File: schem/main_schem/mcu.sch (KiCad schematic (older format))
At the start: 40 parts, among them P2 CONN_PORTD, P3 CONN_ICD, P4 CONN_NFC, P5 CONN_2, Q2 NPN, SW1 SW_RESET, U4 25LC256, U5 PIC18F97J60, X1 25MHz

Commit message: Switch NFC comm from SPI to I2C
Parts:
- added R? (x2): 3.3k, symbol R
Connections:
- net +3.3V: now also R?.1, R?.1
- net SCK1: no longer P4.2 (P2)
- net SDO1: no longer P4.4 (P4)
- net SCL: now reaches P2.6 (P6), U5.84 (RD6/AD6/PSP6/SCK2/SCL2)
- net SCL: now also P4.2 (P2), R?.2
- net SCA: now reaches P2.7 (P7), U5.87 (RD5/AD5/PSP5/SDI2/SDA2)
- net SCA: now also P4.4 (P4), R?.2
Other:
- note removed: "FLIPS RX POLARITY OF ETHERNET"
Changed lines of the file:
@@
-EESchema Schematic File Version 2  date 10/8/2012 1:33:22 PM
+EESchema Schematic File Version 2  date 10/12/2012 9:52:20 AM
 LIBS:power
 LIBS:device
@@
 Sheet 4 6
 Title "MCU block"
-Date "8 oct 2012"
+Date "12 oct 2012"
 Rev "1"
 Comp "ECE 402 Senior Design, Ingersoll Rand Group"
@@
 Comment4 ""
 $EndDescr
-Text Notes 2000 2650 0    30   ~ 0
-for XC1671CT-ND:\n c_l = 18pF\n\nC7=C8=Cb\n\nCb / 2 + (2 to 5 pF) = cl\n27/2 + 3.5 = 17pF --> about 18 pF
-Text Notes 8900 3700 0    60   ~ 0
-BREAKOUT TO EXTERNAL NFC BOARD
+Connection ~ 8500 3700
+Wire Wire Line
+	8500 3700 8500 3650
+Connection ~ 7950 4300
+Wire Wire Line
+	7950 4300 8450 4300
+Wire Wire Line
+	8450 4300 8450 4250
+Wire Wire Line
+	8050 4500 8050 3250
+Connection ~ 7950 3350
 Wire Notes Line
 	11200 5150 8850 5150
@@
 Wire Notes Line
 	8850 3600 11200 3600
+Connection ~ 8050 3250
+Wire Wire Line
+	7950 4500 7950 3350
+Wire Wire Line
+	8600 4250 8600 4350
+Wire Wire Line
+	8600 4350 8050 4350
+Connection ~ 8050 4350
+Wire Wire Line
+	8450 3750 8450 3700
+Wire Wire Line
+	8450 3700 8600 3700
+Wire Wire Line
+	8600 3700 8600 3750
+$Comp
+L +3.3V #PWR?
+U 1 1 50782C27
+P 8500 3650
+F 0 "#PWR?" H 8500 3610 30  0001 C CNN
+F 1 "+3.3V" H 8500 3760 30  0000 C CNN
+	1    8500 3650
+	1    0    0    -1
+$EndComp
+$Comp
+L R R?
+U 1 1 50782BA9
+P 8450 4000
+F 0 "R?" V 8530 4000 50  0000 C CNN
+F 1 "3.3k" V 8450 4000 50  0000 C CNN
+	1    8450 4000
+	1    0    0    -1
+$EndComp
+$Comp
+L R R?
+U 1 1 50782B9F
+P 8600 4000
+F 0 "R?" V 8680 4000 50  0000 C CNN
+F 1 "3.3k" V 8600 4000 50  0000 C CNN
+	1    8600 4000
+	1    0    0    -1
+$EndComp
+Text GLabel 7950 4500 3    30   BiDi ~ 0
+SCA
+Text GLabel 8050 4500 3    30   Output ~ 0
+SCL
+$Comp
+L CONN_8 P2
+U 1 1 506EDDF7
+P 8500 3100
+F 0 "P2" V 8450 3100 60  0000 C CNN
+F 1 "CONN_PORTD" V 8550 3100 60  0000 C CNN
+	1    8500 3100
+	1    0    0    -1
+$EndComp
+Text Notes 2000 2650 0    30   ~ 0
+for XC1671CT-ND:\n c_l = 18pF\n\nC7=C8=Cb\n\nCb / 2 + (2 to 5 pF) = cl\n27/2 + 3.5 = 17pF --> about 18 pF
+Text Notes 8900 3700 0    60   ~ 0
+BREAKOUT TO EXTERNAL NFC BOARD
 Text Notes 5150 7050 0    60   ~ 0
 4kHz PWM sig
@@
 NFC_SELECT_NOT
 Text GLabel 10050 4400 0    60   BiDi ~ 0
-SDO1
+SCA
 Text GLabel 10050 4250 0    60   BiDi ~ 0
 SDI1
 Text GLabel 10050 4100 0    60   BiDi ~ 0
-SCK1
-$Comp
-L CONN_8 P2
-U 1 1 506EDDF7
-P 8500 3100
-F 0 "P2" V 8450 3100 60  0000 C CNN
-F 1 "CONN_PORTD" V 8550 3100 60  0000 C CNN
-	1    8500 3100
-	1    0    0    -1
-$EndComp
+SCL
 $Comp
 L VSS #PWR48
@@
 NoConn ~ 7100 4500
 NoConn ~ 7100 4450
-Text Notes 7300 3950 0    30   ~ 0
-FLIPS RX POLARITY OF ETHERNET
 Text GLabel 7500 4000 2    30   Output ~ 0
 RXSWAP

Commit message: Switch NFC comm from SPI to I2C
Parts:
- gave numbers to parts that had none: 2
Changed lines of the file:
@@
-EESchema Schematic File Version 2  date 10/12/2012 9:52:20 AM
+EESchema Schematic File Version 2  date 10/12/2012 10:11:24 AM
 LIBS:power
 LIBS:device
@@
 Comment4 ""
 $EndDescr
+Text GLabel 10050 4250 0    60   BiDi ~ 0
+SDI1
 Connection ~ 8500 3700
 Wire Wire Line
@@
 	8600 3700 8600 3750
 $Comp
-L +3.3V #PWR?
+L +3.3V #PWR49
 U 1 1 50782C27
 P 8500 3650
-F 0 "#PWR?" H 8500 3610 30  0001 C CNN
+F 0 "#PWR49" H 8500 3610 30  0001 C CNN
 F 1 "+3.3V" H 8500 3760 30  0000 C CNN
 	1    8500 3650
@@
 $EndComp
 $Comp
-L R R?
+L R R22
 U 1 1 50782BA9
 P 8450 4000
-F 0 "R?" V 8530 4000 50  0000 C CNN
+F 0 "R22" V 8530 4000 50  0000 C CNN
 F 1 "3.3k" V 8450 4000 50  0000 C CNN
 	1    8450 4000
@@
 $EndComp
 $Comp
-L R R?
+L R R23
 U 1 1 50782B9F
 P 8600 4000
-F 0 "R?" V 8680 4000 50  0000 C CNN
+F 0 "R23" V 8680 4000 50  0000 C CNN
 F 1 "3.3k" V 8600 4000 50  0000 C CNN
 	1    8600 4000
@@
 NFC_IRQ
 $Comp
-L +3.3V #PWR53
+L +3.3V #PWR54
 U 1 1 507034B9
 P 10350 3950
-F 0 "#PWR53" H 10350 3910 30  0001 C CNN
+F 0 "#PWR54" H 10350 3910 30  0001 C CNN
 F 1 "+3.3V" H 10350 4060 30  0000 C CNN
 	1    10350 3950
@@
 $EndComp
 $Comp
-L VSS #PWR54
+L VSS #PWR55
 U 1 1 506EE8BC
 P 10350 4850
-F 0 "#PWR54" H 10350 4850 30  0001 C CNN
+F 0 "#PWR55" H 10350 4850 30  0001 C CNN
 F 1 "VSS" H 10350 4780 30  0000 C CNN
 	1    10350 4850
@@
 Text GLabel 10050 4400 0    60   BiDi ~ 0
 SCA
-Text GLabel 10050 4250 0    60   BiDi ~ 0
-SDI1
-Text GLabel 10050 4100 0    60   BiDi ~ 0
+Text GLabel 10050 4100 0    60   Input ~ 0
 SCL
 $Comp
@@
 $EndComp
 $Comp
-L VDD #PWR52
+L VDD #PWR53
 U 1 1 506711C2
 P 10000 1950
-F 0 "#PWR52" H 10000 2050 30  0001 C CNN
+F 0 "#PWR53" H 10000 2050 30  0001 C CNN
 F 1 "VDD" H 10000 2060 30  0000 C CNN
 	1    10000 1950
@@
 $EndComp
 $Comp
-L VSS #PWR51
+L VSS #PWR52
 U 1 1 5067114D
 P 9350 2750
-F 0 "#PWR51" H 9350 2750 30  0001 C CNN
+F 0 "#PWR52" H 9350 2750 30  0001 C CNN
 F 1 "VSS" H 9350 2680 30  0000 C CNN
 	1    9350 2750
@@
 $EndComp
 $Comp
-L VSS #PWR55
+L VSS #PWR56
 U 1 1 506710A1
 P 10650 5900
-F 0 "#PWR55" H 10650 5900 30  0001 C CNN
+F 0 "#PWR56" H 10650 5900 30  0001 C CNN
 F 1 "VSS" H 10650 5830 30  0000 C CNN
 	1    10650 5900
@@
 $EndComp
 $Comp
-L VSS #PWR56
+L VSS #PWR57
 U 1 1 5067109D
 P 10650 6450
-F 0 "#PWR56" H 10650 6450 30  0001 C CNN
+F 0 "#PWR57" H 10650 6450 30  0001 C CNN
 F 1 "VSS" H 10650 6380 30  0000 C CNN
 	1    10650 6450
@@
 NoConn ~ 10300 1450
 $Comp
-L VSS #PWR50
+L VSS #PWR51
 U 1 1 50670828
 P 8800 1500
-F 0 "#PWR50" H 8800 1500 30  0001 C CNN
+F 0 "#PWR51" H 8800 1500 30  0001 C CNN
 F 1 "VSS" H 8800 1430 30  0000 C CNN
 	1    8800 1500
@@
 $EndComp
 $Comp
-L +3.3V #PWR49
+L +3.3V #PWR50
 U 1 1 50670805
 P 8800 800
-F 0 "#PWR49" H 8800 760 30  0001 C CNN
+F 0 "#PWR50" H 8800 760 30  0001 C CNN
 F 1 "+3.3V" H 8800 910 30  0000 C CNN
 	1    8800 800

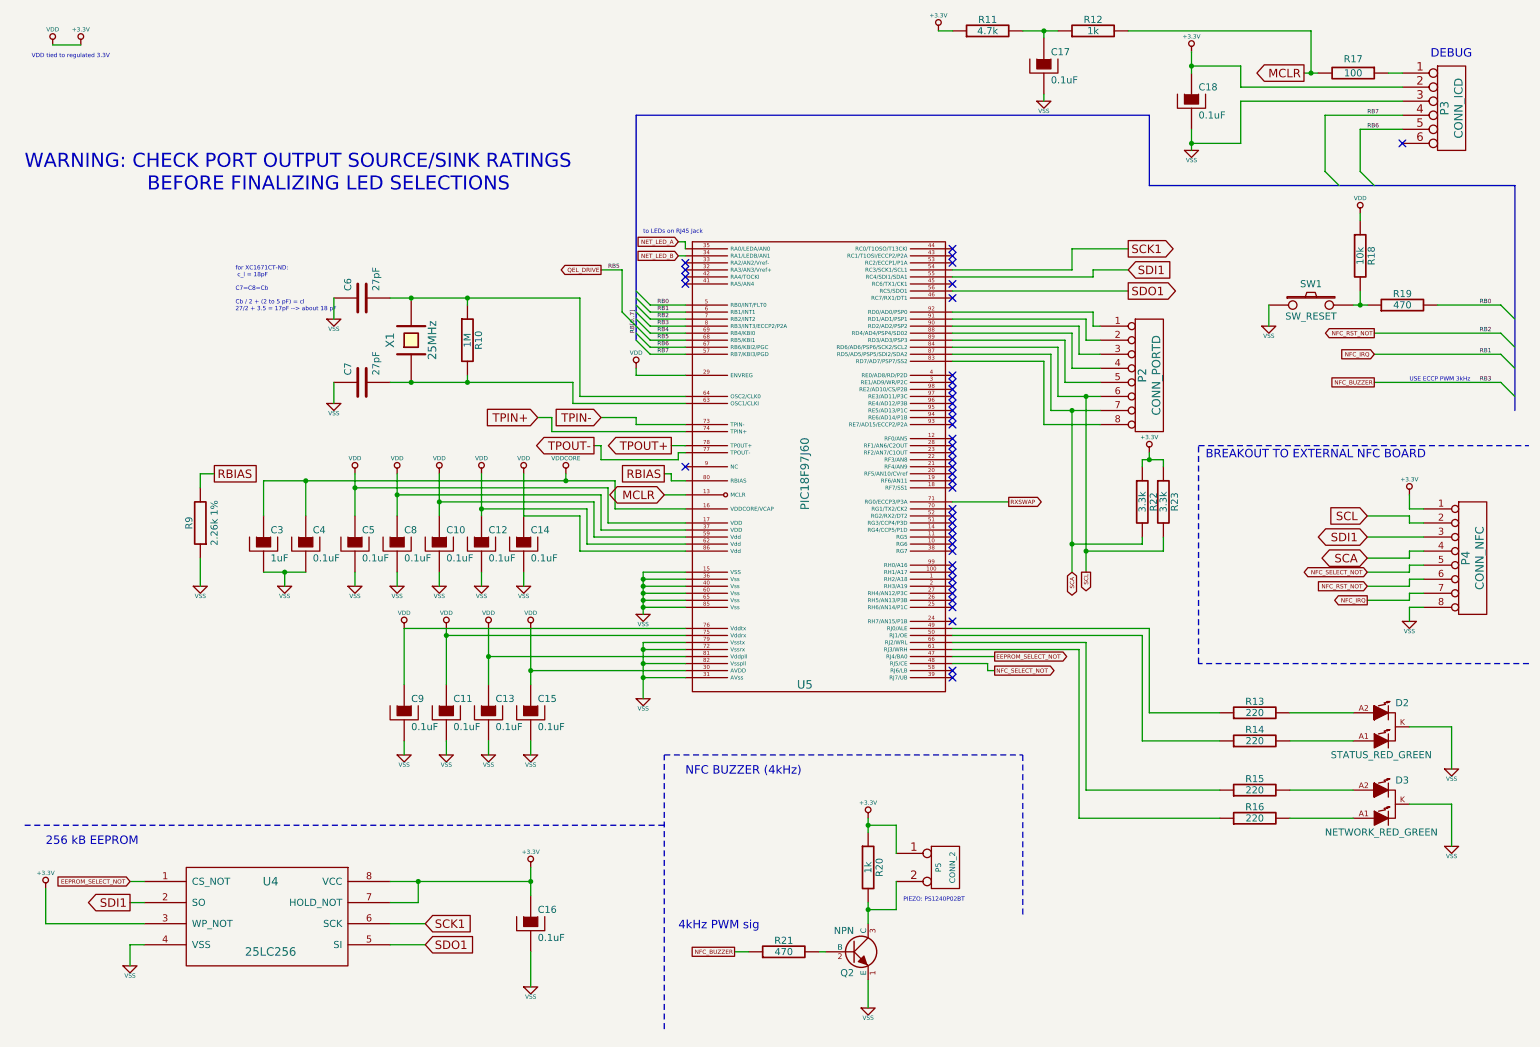
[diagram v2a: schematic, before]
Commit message: Latest update of board, footprints match except for LEDs
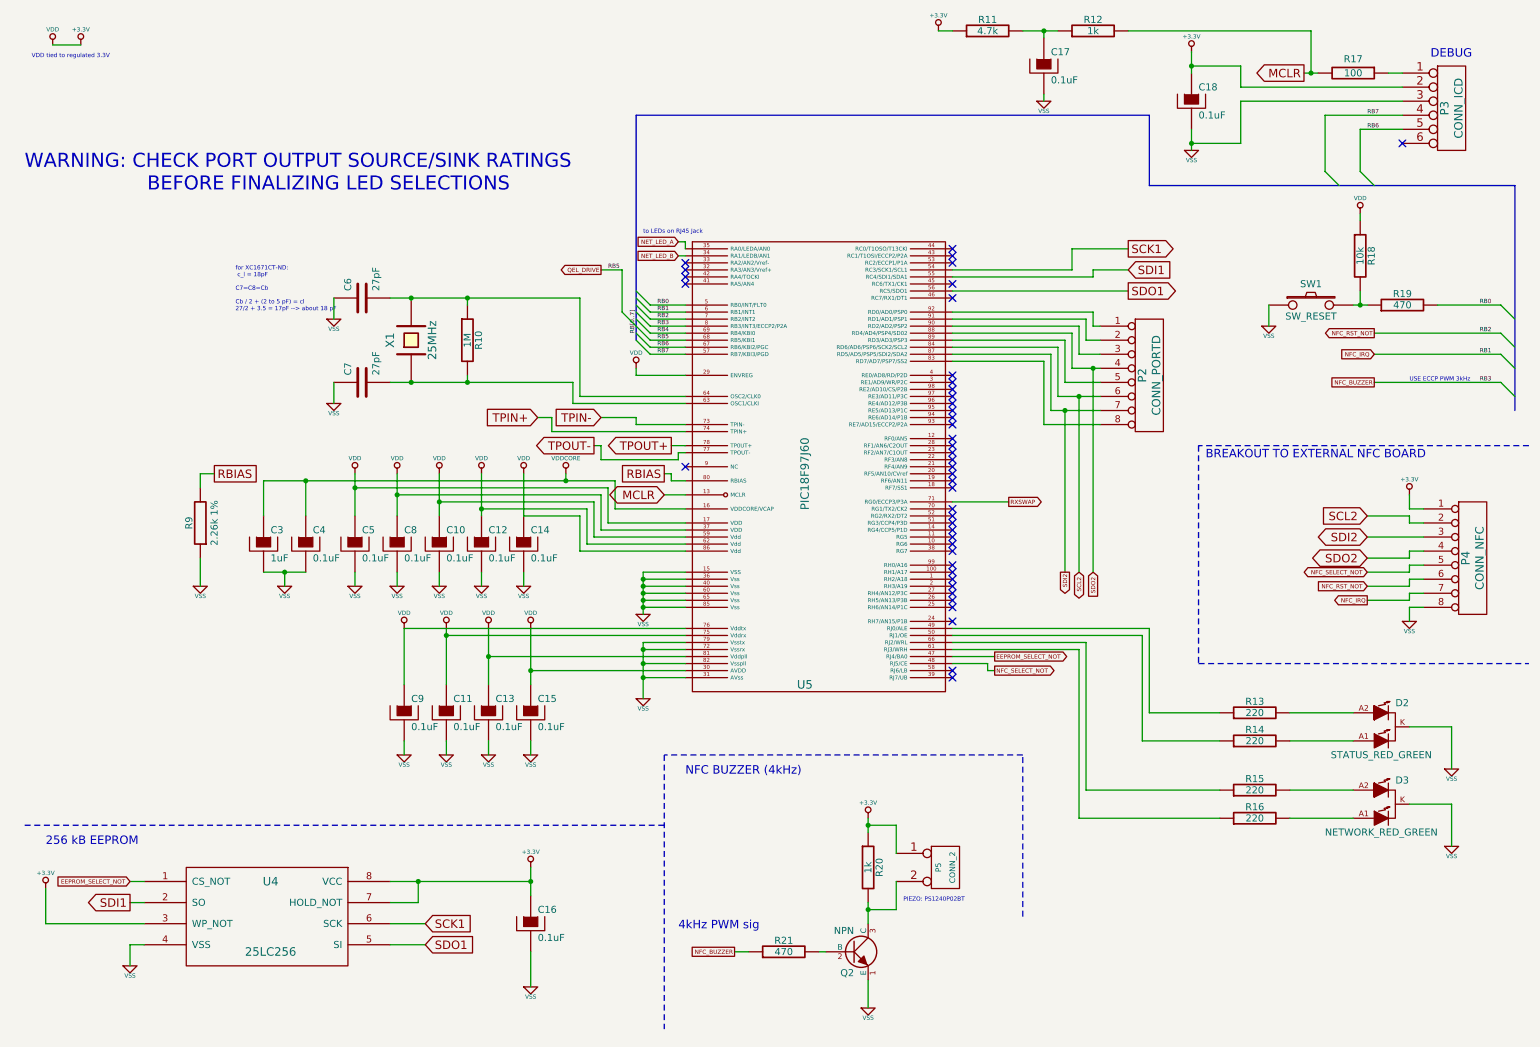
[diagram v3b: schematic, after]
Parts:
- removed R22, R23: 3.3k, symbol R
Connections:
- net SDI1: no longer P4.3 (P3)
- net SDO2: now reaches P2.4 (P4), U5.88 (RD4/AD4/PSP4/SD02)
- net SDO2: now also P4.4 (P4)
- net SCA renamed SDI2
- net SDI2: now also P4.3 (P3); no longer P4.4 (P4)
- net SCL renamed SCL2

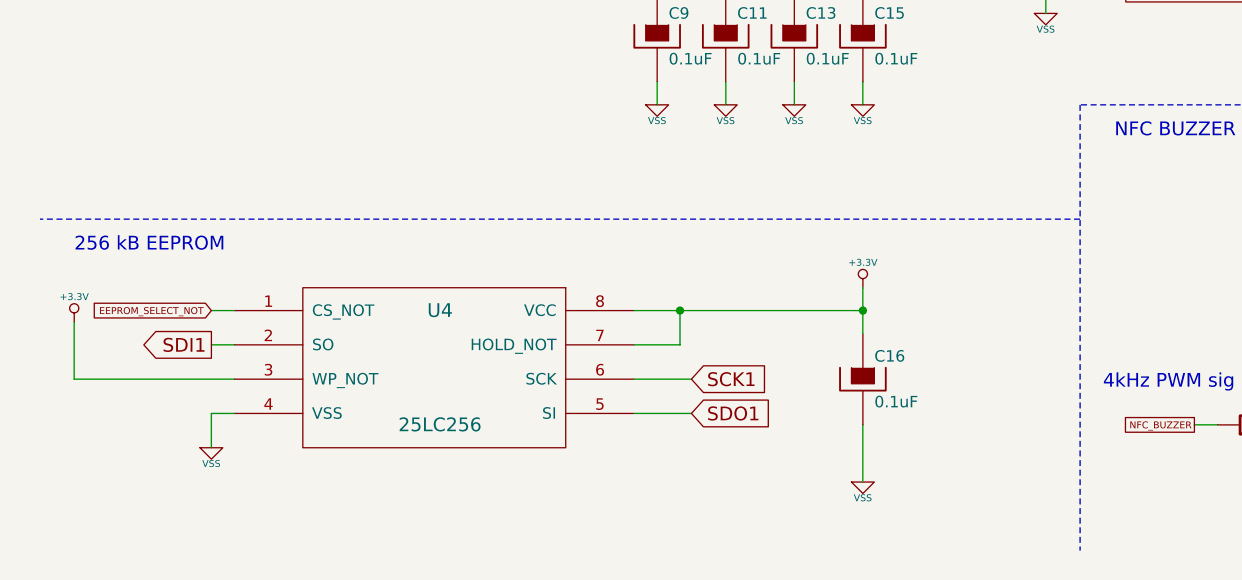
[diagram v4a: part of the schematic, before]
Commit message: Power connector, update led footprint, update TODO, route power traces
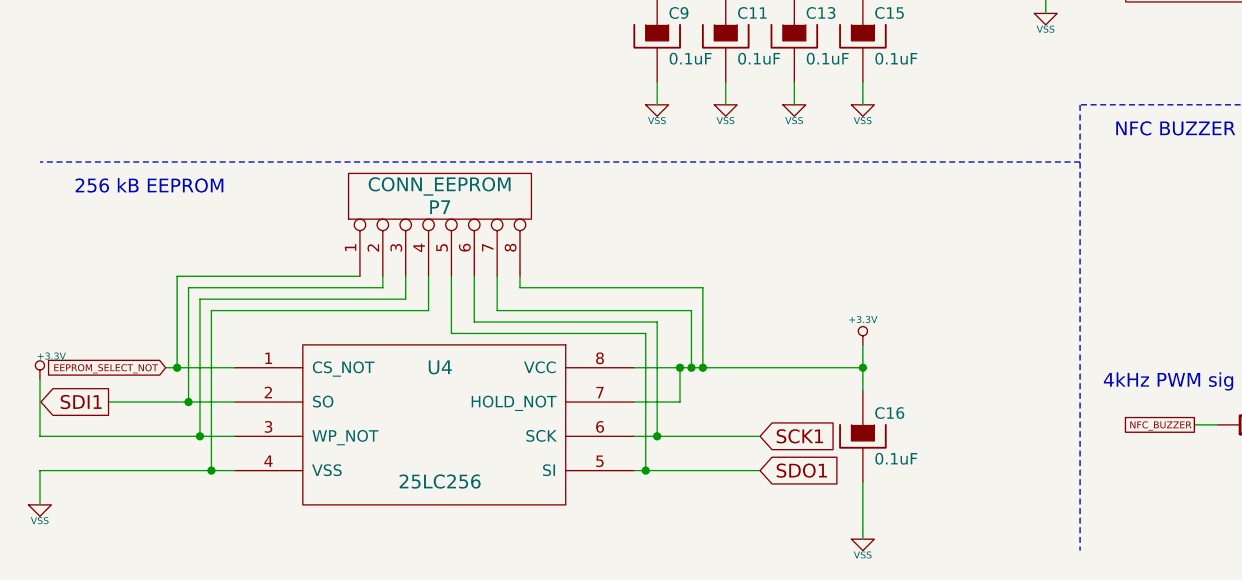
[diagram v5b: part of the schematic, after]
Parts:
- added P7: CONN_EEPROM, symbol CONN_8
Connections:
- net +3.3V: now also P7.3 (P3), P7.7 (P7), P7.8 (P8)
- net EEPROM_SELECT_NOT: now also P7.1 (P1)
- net SCK1: now also P7.6 (P6)
- net SDI1: now also P7.2 (P2)
- net SDO1: now also P7.5 (P5)
- net VSS: now also P7.4 (P4)
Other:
- moved on the sheet: C16, U4

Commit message: Not sure what's in here but need it
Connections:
- net +3.3V: no longer P4.1 (P1)
- new net +5V: P4.1 (P1)
